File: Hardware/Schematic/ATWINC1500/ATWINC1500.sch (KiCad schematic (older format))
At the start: 1 part, among them U1 ATWINC1500-MR210UB

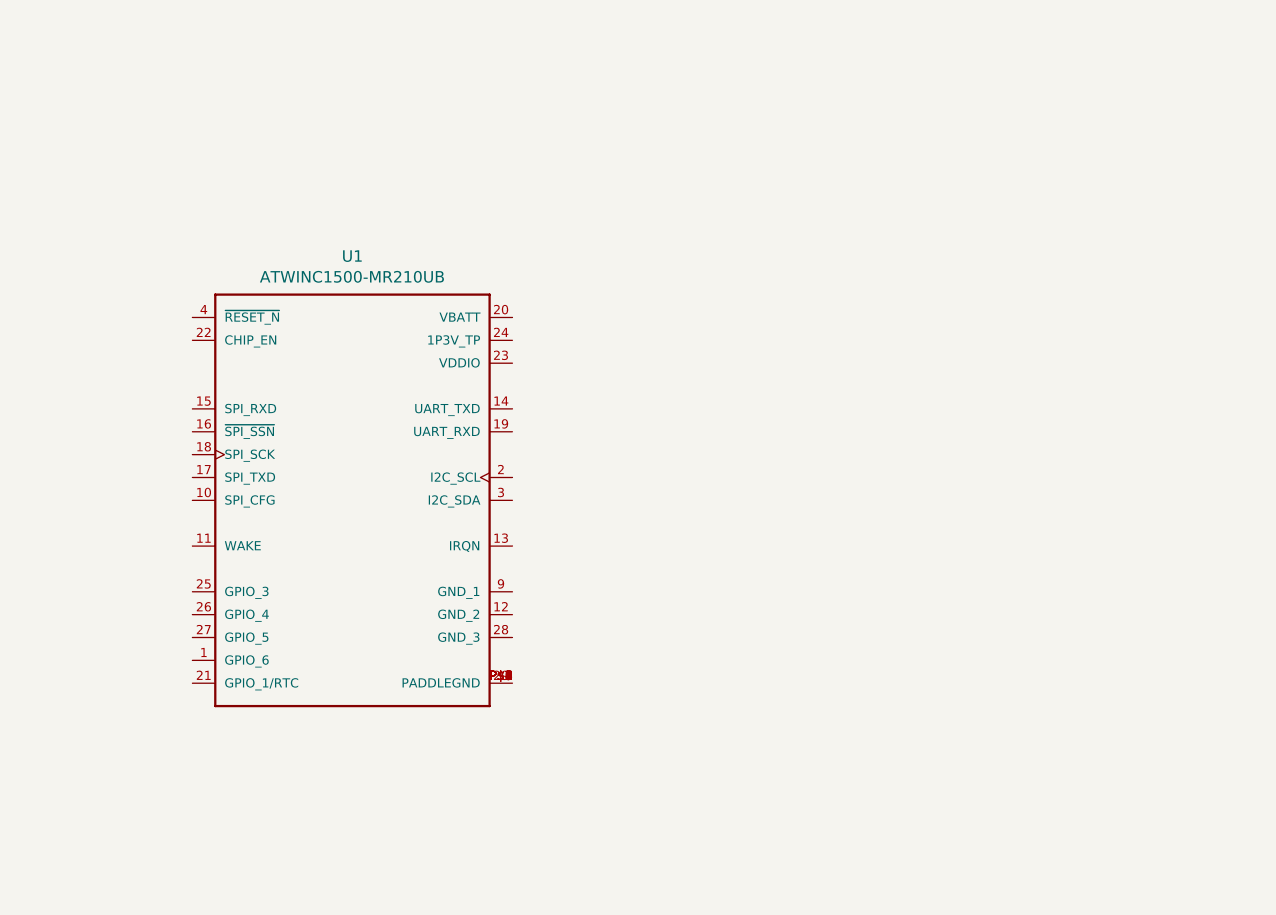
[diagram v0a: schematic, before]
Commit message: Added STM32L496xx datasheet and added symbol to schematic
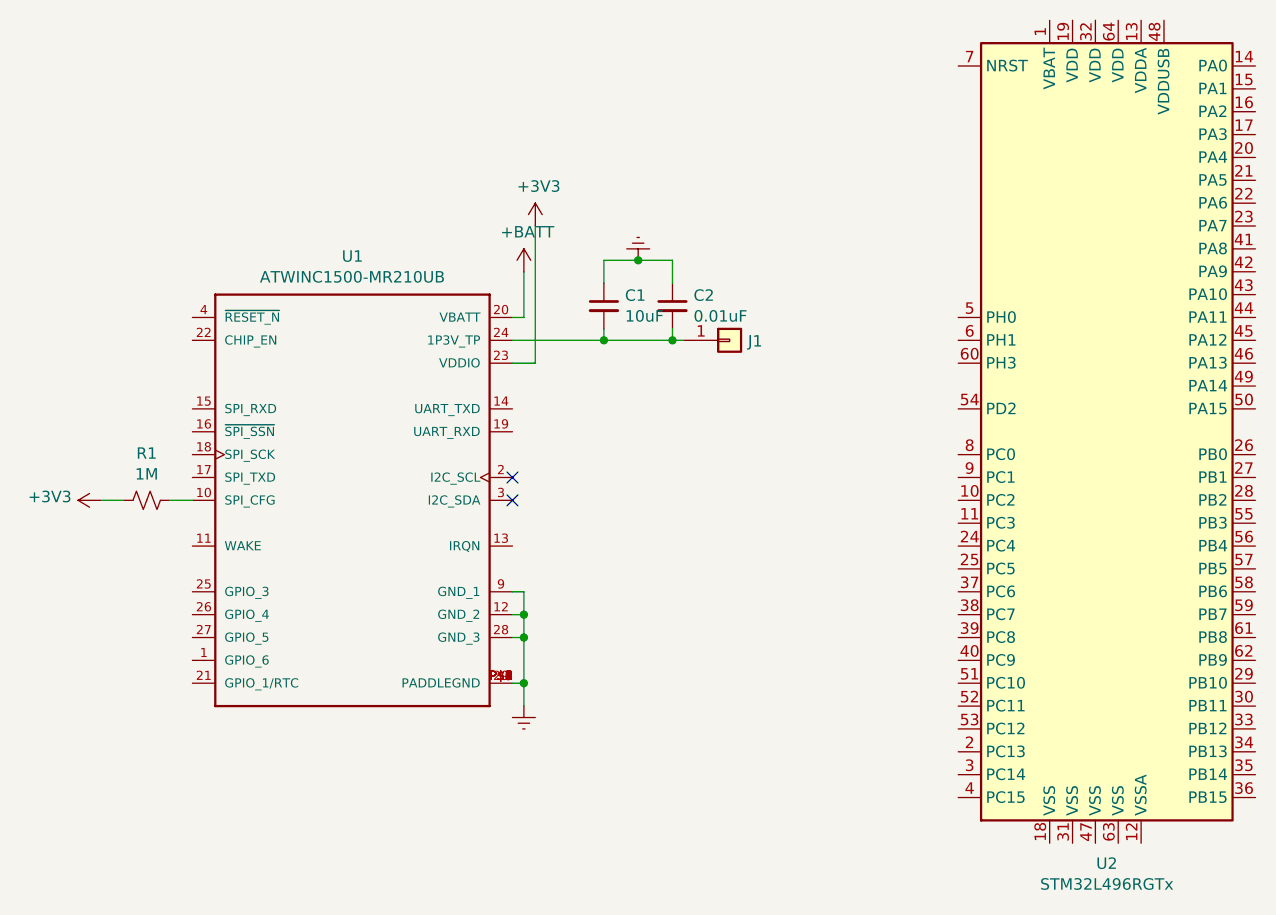
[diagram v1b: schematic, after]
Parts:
- added C1: 10uF, Capacitor_SMD:C_2512_6332Metric_Pad1.52x3.35mm_HandSolder, symbol Device:C_Small
- added C2: 0.01uF, Capacitor_SMD:C_2512_6332Metric_Pad1.52x3.35mm_HandSolder, symbol Device:C_Small
- added J1: Conn_01x01, TestPoint:TestPoint_Pad_1.0x1.0mm, symbol Connector_Generic:Conn_01x01
- added R1: 1M, Resistor_SMD:R_2512_6332Metric_Pad1.52x3.35mm_HandSolder, symbol Device:R_Small_US
- added U2: STM32L496RGTx, Package_QFP:LQFP-64_10x10mm_P0.5mm, symbol MCU_ST_STM32L4:STM32L496RGTx
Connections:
- net at U1.10 (SPI_CFG): now also R1.1
- net Earth: now reaches U1.12 (GND_2)
- net Earth: now also U1.28 (GND_3), U1.29 (PADDLEGND), U1.9 (GND_1), U1.P$1 (PADDLEGND), U1.P$2 (PADDLEGND), U1.P$3 (PADDLEGND), U1.P$4 (PADDLEGND), U1.P$5 (PADDLEGND), U1.P$6 (PADDLEGND), U1.P$7 (PADDLEGND), U1.P$8 (PADDLEGND), U1.P$9 (PADDLEGND), C1.1, C2.1
- net +BATT: now reaches U1.20 (VBATT)
- net +3V3: now reaches U1.23 (VDDIO)
- net +3V3: now also R1.2
- net at U1.24 (1P3V_TP): now also C1.2, C2.2, J1.1 (Pin_1)
- no-connect marks 0 -> 2
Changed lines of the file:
@@
+	1    0    0    -1
+$EndComp
+NoConn ~ 6250 3850
+NoConn ~ 6250 3950
+$Comp
+L power:Earth #PWR0101
+U 1 1 5D0E43CE
+P 6300 4850
+F 0 "#PWR0101" H 6300 4600 50  0001 C CNN
+F 1 "Earth" H 6300 4700 50  0001 C CNN
+F 2 "" H 6300 4850 50  0001 C CNN
+F 3 "~" H 6300 4850 50  0001 C CNN
+	1    6300 4850
+	1    0    0    -1
+$EndComp
+Wire Wire Line
+	6250 4350 6300 4350
+Wire Wire Line
+	6300 4350 6300 4450
+Wire Wire Line
+	6250 4750 6300 4750
+Connection ~ 6300 4750
+Wire Wire Line
+	6300 4750 6300 4850
+Wire Wire Line
+	6250 4550 6300 4550
+Connection ~ 6300 4550
+Wire Wire Line
+	6300 4550 6300 4750
+Wire Wire Line
+	6250 4450 6300 4450
+Connection ~ 6300 4450
+Wire Wire Line
+	6300 4450 6300 4550
+$Comp
+L power:+BATT #PWR0102
+U 1 1 5D0E5845
+P 6300 2950
+F 0 "#PWR0102" H 6300 2800 50  0001 C CNN
+F 1 "+BATT" H 6315 3123 50  0000 C CNN
+F 2 "" H 6300 2950 50  0001 C CNN
+F 3 "" H 6300 2950 50  0001 C CNN
+	1    6300 2950
+	1    0    0    -1
+$EndComp
+Wire Wire Line
+	6300 3150 6300 2950
+$Comp
+L power:+3V3 #PWR0103
+U 1 1 5D0E6F7C
+P 6350 2750
+F 0 "#PWR0103" H 6350 2600 50  0001 C CNN
+F 1 "+3V3" H 6365 2923 50  0000 C CNN
+F 2 "" H 6350 2750 50  0001 C CNN
+F 3 "" H 6350 2750 50  0001 C CNN
+	1    6350 2750
+	1    0    0    -1
+$EndComp
+$Comp
+L Device:R_Small_US R1
+U 1 1 5D0E876B
+P 4650 3950
+F 0 "R1" V 4445 3950 50  0000 C CNN
+F 1 "1M" V 4536 3950 50  0000 C CNN
+F 2 "Resistor_SMD:R_2512_6332Metric_Pad1.52x3.35mm_HandSolder" H 4650 3950 50  0001 C CNN
+F 3 "~" H 4650 3950 50  0001 C CNN
+	1    4650 3950
+	0    1    1    0
+$EndComp
+Wire Wire Line
+	4750 3950 4850 3950
+Wire Wire Line
+	4550 3950 4450 3950
+$Comp
+L power:+3V3 #PWR0104
+U 1 1 5D0E99FF
+P 4450 3950
+F 0 "#PWR0104" H 4450 3800 50  0001 C CNN
+F 1 "+3V3" V 4465 4078 50  0000 L CNN
+F 2 "" H 4450 3950 50  0001 C CNN
+F 3 "" H 4450 3950 50  0001 C CNN
+	1    4450 3950
+	0    -1   -1   0
+$EndComp
+$Comp
+L Device:C_Small C1
+U 1 1 5D0EBEA5
+P 6650 3100
+F 0 "C1" H 6742 3146 50  0000 L CNN
+F 1 "10uF" H 6742 3055 50  0000 L CNN
+F 2 "Capacitor_SMD:C_2512_6332Metric_Pad1.52x3.35mm_HandSolder" H 6650 3100 50  0001 C CNN
+F 3 "~" H 6650 3100 50  0001 C CNN
+	1    6650 3100
+	1    0    0    -1
+$EndComp
+Wire Wire Line
+	6250 3150 6300 3150
+Wire Wire Line
+	6250 3350 6350 3350
+Wire Wire Line
+	6350 2750 6350 3350
+$Comp
+L Device:C_Small C2
+U 1 1 5D0EE3CD
+P 6950 3100
+F 0 "C2" H 7042 3146 50  0000 L CNN
+F 1 "0.01uF" H 7042 3055 50  0000 L CNN
+F 2 "Capacitor_SMD:C_2512_6332Metric_Pad1.52x3.35mm_HandSolder" H 6950 3100 50  0001 C CNN
+F 3 "~" H 6950 3100 50  0001 C CNN
+	1    6950 3100
+	1    0    0    -1
+$EndComp
+$Comp
+L power:Earth #PWR0105
+U 1 1 5D0EF94B
+P 6800 2900
+F 0 "#PWR0105" H 6800 2650 50  0001 C CNN
+F 1 "Earth" H 6800 2750 50  0001 C CNN
+F 2 "" H 6800 2900 50  0001 C CNN
+F 3 "~" H 6800 2900 50  0001 C CNN
+	1    6800 2900
+	-1   0    0    1
+$EndComp
+Wire Wire Line
+	6250 3250 6650 3250
+Wire Wire Line
+	6950 3250 6950 3200
+Wire Wire Line
+	6650 3200 6650 3250
+Wire Wire Line
+	6650 3000 6650 2900
+Wire Wire Line
+	6650 2900 6800 2900
+Wire Wire Line
+	6950 3000 6950 2900
+Wire Wire Line
+	6950 2900 6800 2900
+Connection ~ 6800 2900
+Wire Wire Line
+	6950 3250 7000 3250
+Connection ~ 6950 3250
+Connection ~ 6650 3250
+Wire Wire Line
+	6650 3250 6950 3250
+$Comp
+L Connector_Generic:Conn_01x01 J1
+U 1 1 5D0F180E
+P 7200 3250
+F 0 "J1" H 7280 3246 50  0000 L CNN
+F 1 "Conn_01x01" H 7280 3201 50  0001 L CNN
+F 2 "TestPoint:TestPoint_Pad_1.0x1.0mm" H 7200 3250 50  0001 C CNN
+F 3 "~" H 7200 3250 50  0001 C CNN
+	1    7200 3250
+	1    0    0    -1
+$EndComp
+$Comp
+L MCU_ST_STM32L4:STM32L496RGTx U2
+U 1 1 5D10F496
+P 8900 3650
+F 0 "U2" H 8850 1761 50  0000 C CNN
+F 1 "STM32L496RGTx" H 8850 1670 50  0000 C CNN
+F 2 "Package_QFP:LQFP-64_10x10mm_P0.5mm" H 8300 1950 50  0001 R CNN
+F 3 "http://www.st.com/st-web-ui/static/active/en/resource/technical/document/datasheet/DM00284211.pdf" H 8900 3650 50  0001 C CNN
+	1    8900 3650
 	1    0    0    -1
 $EndComp
